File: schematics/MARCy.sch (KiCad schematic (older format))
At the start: 3 parts, among them J2 JTAG, U3 XC9572XL-TQ100

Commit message: Use the right component, idiot...
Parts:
- removed R?: 0.1uF, symbol Device:R_Small
- added C?: 0.1uF, symbol Device:C
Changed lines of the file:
@@
 Text HLabel 5700 1950 2    50   Input ~ 0
 A[0..15]
-Text HLabel 7300 1000 0    50   Input ~ 0
-Vcc33
-$Comp
-L Device:R_Small R?
-U 1 1 5F14E0B3
-P 7450 1100
-F 0 "R?" H 7509 1146 50  0000 L CNN
-F 1 "0.1uF" H 7509 1055 50  0000 L CNN
-F 2 "" H 7450 1100 50  0001 C CNN
-F 3 "~" H 7450 1100 50  0001 C CNN
-	1    7450 1100
-	1    0    0    -1
-$EndComp
-Wire Wire Line
-	7300 1000 7450 1000
-Wire Wire Line
-	7450 1000 7800 1000
-Connection ~ 7450 1000
-Text HLabel 7300 1200 0    50   Input ~ 0
-GND
-Text GLabel 7800 1000 2    50   Output ~ 0
-Vcc33
-Text GLabel 7800 1200 2    50   Output ~ 0
-GND
-Wire Wire Line
-	7800 1200 7450 1200
-Wire Wire Line
-	7300 1200 7450 1200
-Connection ~ 7450 1200
 Text GLabel 5400 750  2    50   Input ~ 0
 Vcc33
@@
 Wire Wire Line
 	2300 5200 2950 5200
+Text HLabel 8250 3450 0    50   Input ~ 0
+GND
+$Comp
+L Device:C C?
+U 1 1 61660BC5
+P 8550 3300
+F 0 "C?" H 8665 3346 50  0000 L CNN
+F 1 "0.1uF" H 8665 3255 50  0000 L CNN
+F 2 "" H 8588 3150 50  0001 C CNN
+F 3 "~" H 8550 3300 50  0001 C CNN
+	1    8550 3300
+	1    0    0    -1
+$EndComp
+Wire Wire Line
+	8250 3150 8550 3150
+Wire Wire Line
+	8250 3450 8550 3450
+Text GLabel 9000 3450 2    50   Input ~ 10
+GND
+Text HLabel 8250 3150 0    50   Input ~ 0
+Vcc33
+Text GLabel 9000 3150 2    50   Input ~ 0
+Vcc33
+Wire Wire Line
+	8550 3450 9000 3450
+Connection ~ 8550 3450
+Wire Wire Line
+	8550 3150 9000 3150
+Connection ~ 8550 3150
 Wire Bus Line
 	5600 1950 5600 3450

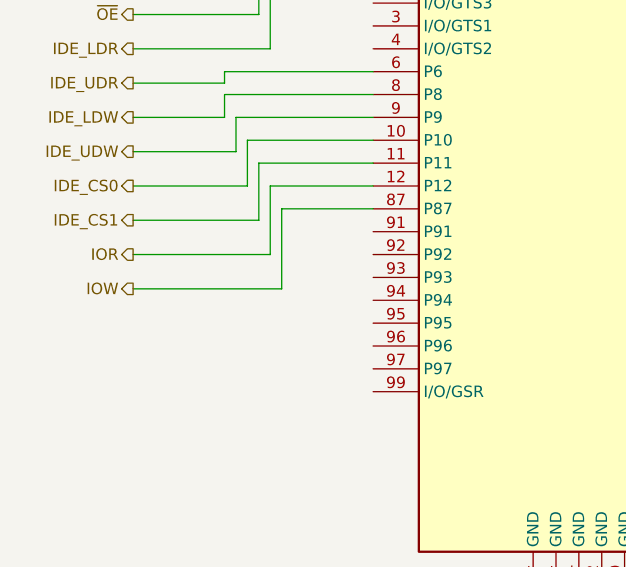
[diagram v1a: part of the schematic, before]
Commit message: Opposite PHI2 and RWB trigger bank address on d0..7
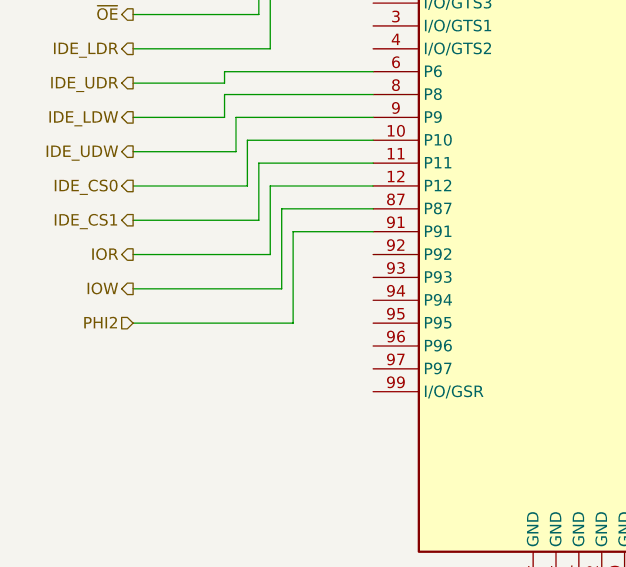
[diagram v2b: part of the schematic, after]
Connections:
- net labels added: PHI2
- wire segments 164 -> 167
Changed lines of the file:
@@
 	8550 3150 9000 3150
 Connection ~ 8550 3150
+Text HLabel 2300 5350 0    50   Input ~ 0
+PHI2
+Wire Wire Line
+	3350 4950 3000 4950
+Wire Wire Line
+	3000 4950 3000 5350
+Wire Wire Line
+	3000 5350 2300 5350
 Wire Bus Line
 	5600 1950 5600 3450

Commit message: Just so I don't forget...
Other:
- note added: "This pin needs to be negated\nfor Bus Address decoding! >>>"
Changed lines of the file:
@@
 Wire Bus Line
 	5600 3850 5600 5000
+Text Notes 800  5400 0    50   ~ 0
+This pin needs to be negated\nfor Bus Address decoding! >>>
 $EndSCHEMATC

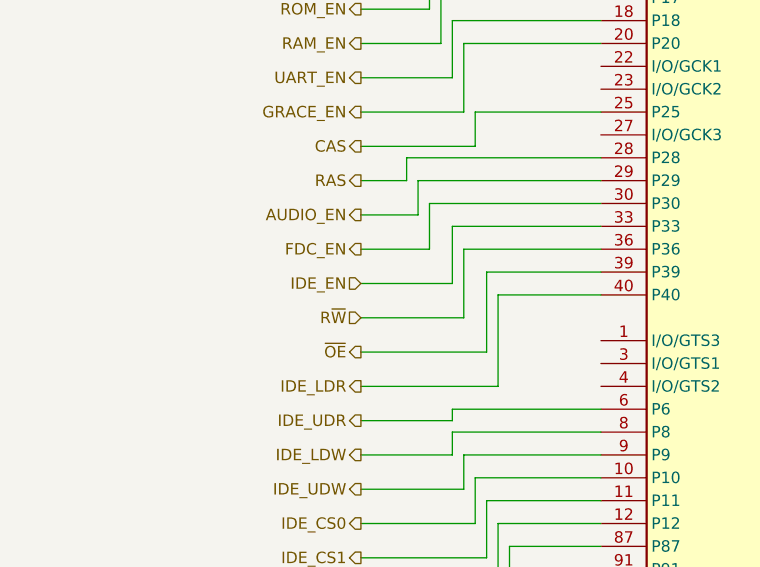
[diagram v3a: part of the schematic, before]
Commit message: begin wiring up the hierarchial sheets
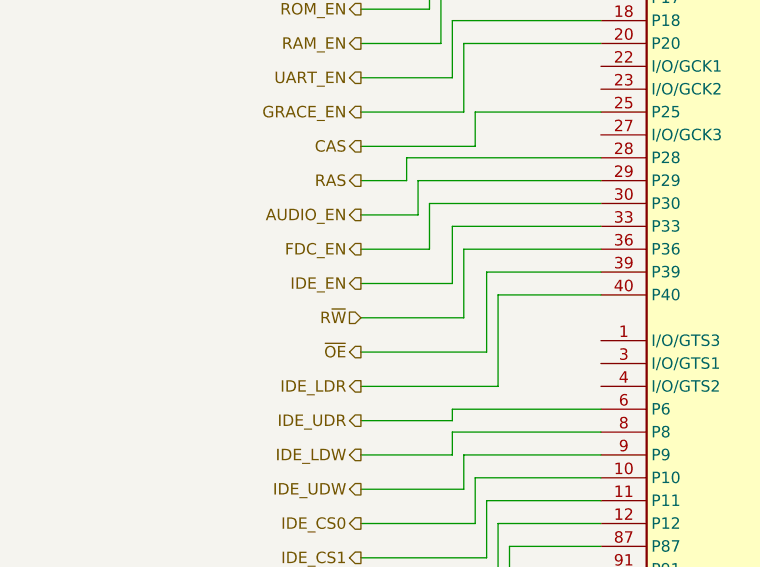
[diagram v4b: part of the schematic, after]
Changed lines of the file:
@@
 Wire Wire Line
 	2300 3550 2600 3550
-Text HLabel 2300 3700 0    50   Input ~ 0
+Text HLabel 2300 3700 0    50   Output ~ 0
 IDE_EN
 Wire Wire Line

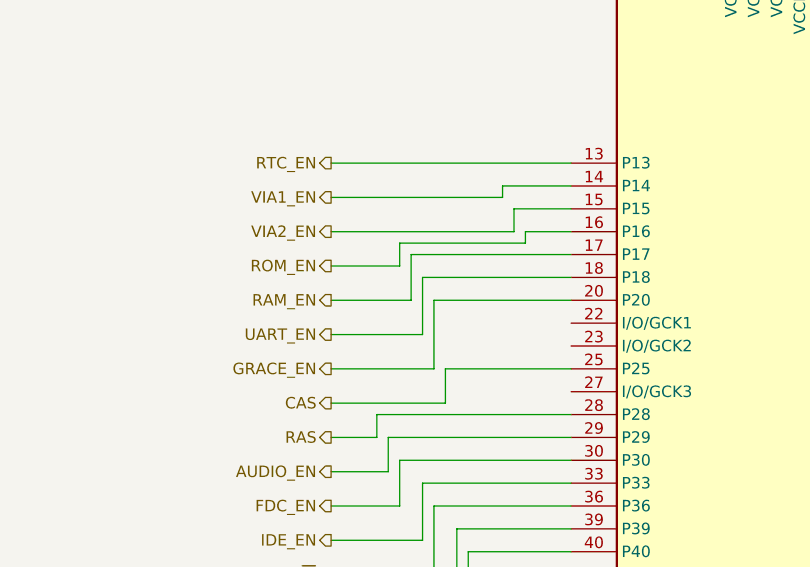
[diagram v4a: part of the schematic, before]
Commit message: Issue #4: Remove RAM_EN pin
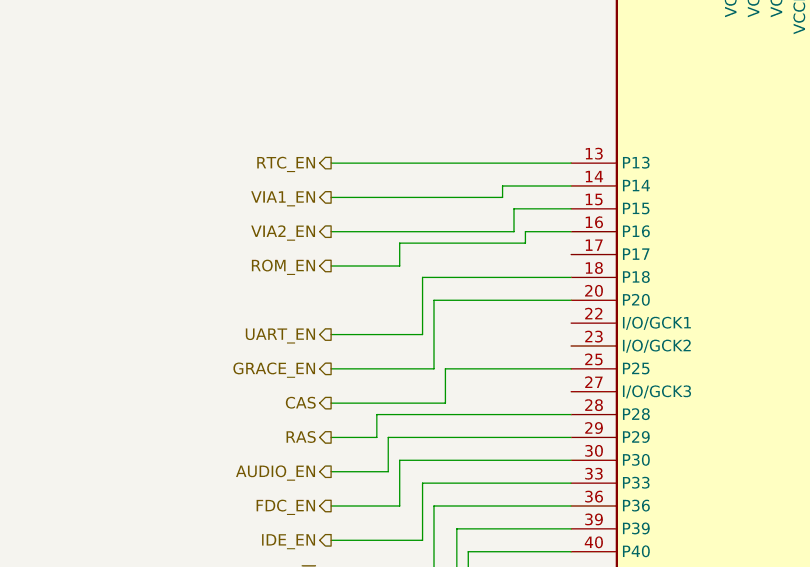
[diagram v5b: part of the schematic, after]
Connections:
- net labels removed: RAM_EN
- wire segments 167 -> 164
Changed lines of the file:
@@
 	2600 2400 3150 2400
-Wire Wire Line
-	2650 2450 2650 2650
-Wire Wire Line
-	2650 2450 3350 2450
 Wire Wire Line
 	2700 2550 2700 2800
@@
 Text HLabel 2300 2500 0    50   Output ~ 0
 ROM_EN
-Text HLabel 2300 2650 0    50   Output ~ 0
-RAM_EN
 Text HLabel 2300 2800 0    50   Output ~ 0
 UART_EN
@@
 	2300 2500 2600 2500
 Wire Wire Line
-	2300 2650 2650 2650
-Wire Wire Line
 	2300 2800 2700 2800
